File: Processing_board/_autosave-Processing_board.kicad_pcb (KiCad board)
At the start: 4 copper layers, 95.2 x 62 mm, 116 parts, among them J1 Conn_01x08_Pin, J10 Conn_01x03_Pin, J11 CONMHF1-SMD-G-T, J2 Conn_01x08_Pin, J3 Conn_01x06_Pin, J4 Conn_01x03_Pin, J5 Conn_01x03_Pin, J6 Conn_01x02_Pin, J7 Conn_01x02_Pin, J8 USB4215-03-A_REVA, J9 Conn_01x03_Pin, Q1 DMN66D0LT-7, Q2 DMN66D0LT-7, Q3 DMP3056LSS-13, SW1 TL3305BF100QG, SW2 TL3305BF100QG, U1 STM32WBA63CIU6, U2 MCP2200-I_SO, U3 LD1117S50TR_SOT223, U4 LD1117S33TR_SOT223, U5 LD1117DT18TR, U6 BGS13SN8E6327XTSA1, U7 OPA192IDR, U8 REF5025AQDRQ1, U9 ADS7953SBDBT

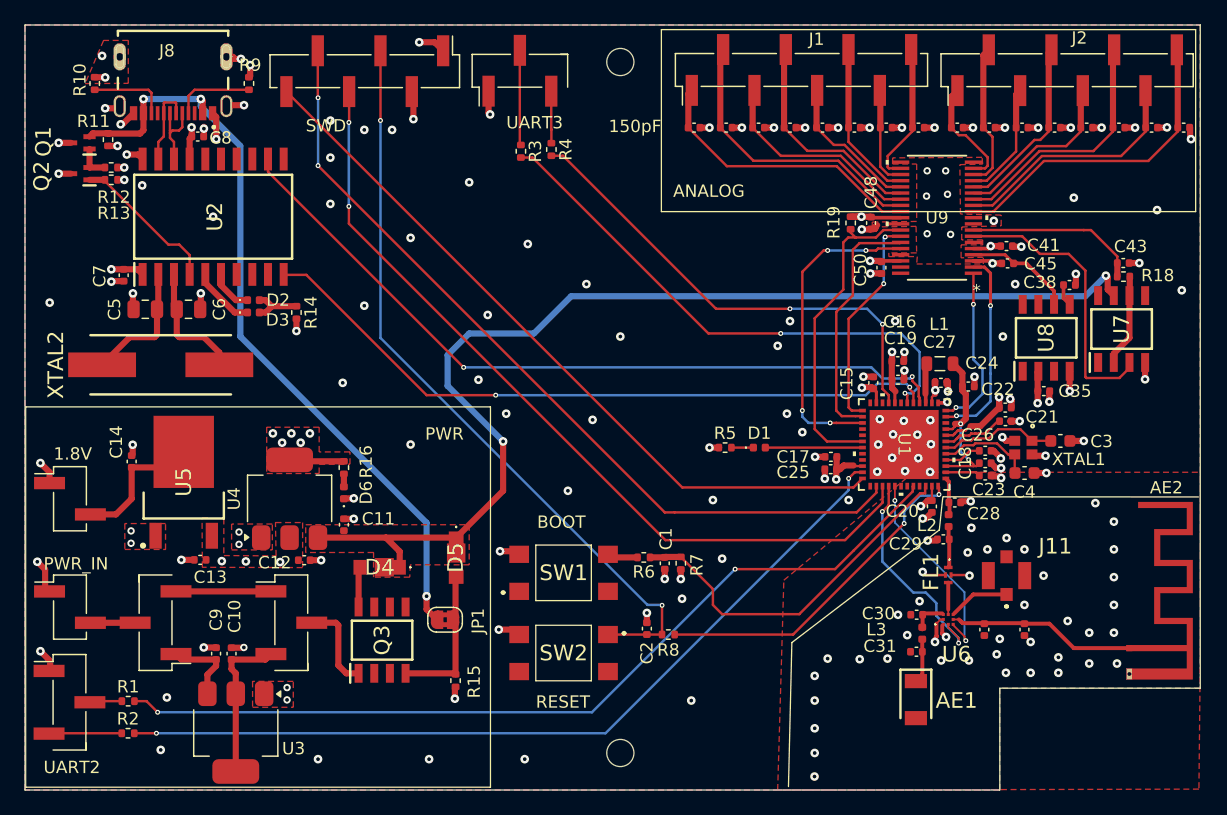
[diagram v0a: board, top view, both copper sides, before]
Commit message: minor changes to correct DRC warnings
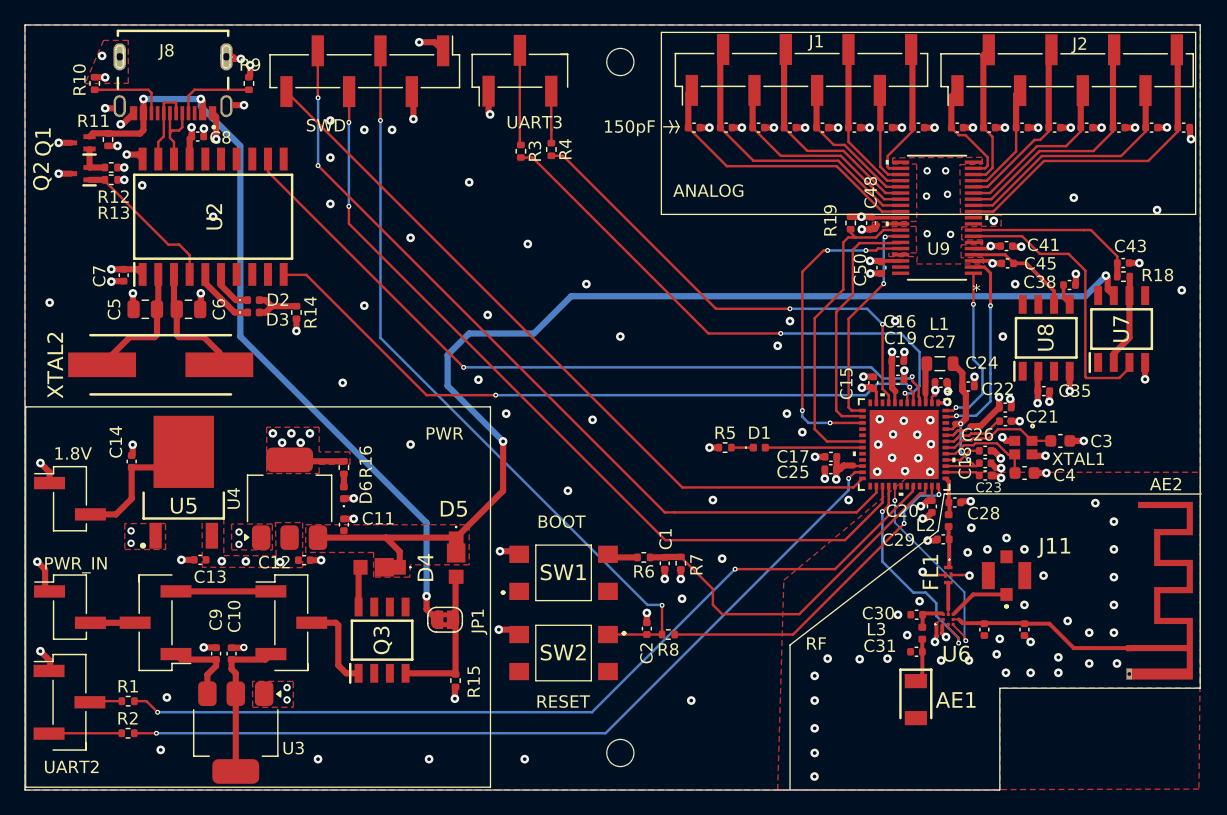
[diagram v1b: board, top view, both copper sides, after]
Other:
- board text added: "RF"
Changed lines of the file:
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@@
 		(tags "PCB antenna")
 		(property "Reference" "AE2"
-			(at -13 -3 180)
+			(at -13.25 -3 180)
 			(layer "F.SilkS")
 			(effects
@@
 		(tags "capacitor")
 		(property "Reference" "C29"
-			(at 3.074651 -0.367158 180)
+			(at 3.624651 -0.067158 180)
 			(layer "F.SilkS")
 			(effects
@@
 		(tags "capacitor")
 		(property "Reference" "C4"
-			(at 0.01 -1.54 0)
+			(at -3.24 -0.19 0)
 			(layer "F.SilkS")
 			(effects
@@
 		(tags "ADS7953SBDBT ")
 		(property "Reference" "U9"
-			(at 0 0 0)
+			(at -0.134931 -2.530498 0)
 			(unlocked yes)
 			(layer "F.SilkS")
@@
 		(tags "Integrated Circuit")
 		(property "Reference" "U5"
-			(at 0 0 90)
+			(at -1.955 0 180)
 			(layer "F.SilkS")
 			(effects
@@
 			(pinfunction "GND_A")
 			(pintype "power_in")
-			(solder_mask_margin 0.102)
+			(solder_mask_margin 0.09)
 		)
 		(pad "A4_B9" smd rect
@@
 			(pinfunction "VBUS_A")
 			(pintype "power_in")
-			(solder_mask_margin 0.102)
+			(solder_mask_margin 0.09)
 		)
 		(pad "A5" smd rect
@@
 			(pinfunction "CC1")
 			(pintype "bidirectional")
-			(solder_mask_margin 0.102)
+			(solder_mask_margin 0.09)
 		)
 		(pad "A6" smd rect
@@
 			(pinfunction "D+")
 			(pintype "bidirectional")
-			(solder_mask_margin 0.102)
+			(solder_mask_margin 0.09)
 		)
 		(pad "A7" smd rect
@@
 			(pinfunction "D-")
 			(pintype "bidirectional")
-			(solder_mask_margin 0.102)
+			(solder_mask_margin 0.09)
 		)
 		(pad "A8" smd rect
@@
 			(pinfunction "SBU1")
 			(pintype "bidirectional+no_connect")
-			(solder_mask_margin 0.102)
+			(solder_mask_margin 0.09)
 		)
 		(pad "B1_A12" smd rect
@@
 			(pinfunction "GND_B")
 			(pintype "power_in")
-			(solder_mask_margin 0.102)
+			(solder_mask_margin 0.09)
 		)
 		(pad "B4_A9" smd rect
@@
 			(pinfunction "VBUS_B")
 			(pintype "power_in")
-			(solder_mask_margin 0.102)
+			(solder_mask_margin 0.09)
 		)
 		(pad "B5" smd rect
@@
 			(pinfunction "CC2")
 			(pintype "bidirectional")
-			(solder_mask_margin 0.102)
+			(solder_mask_margin 0.09)
 		)
 		(pad "B6" smd rect
@@
 			(pinfunction "D+")
 			(pintype "bidirectional")
-			(solder_mask_margin 0.102)
+			(solder_mask_margin 0.09)
 		)
 		(pad "B7" smd rect
@@
 			(pinfunction "D-")
 			(pintype "bidirectional")
-			(solder_mask_margin 0.102)
+			(solder_mask_margin 0.09)
 		)
 		(pad "B8" smd rect
@@
 			(pinfunction "SBU2")
 			(pintype "bidirectional+no_connect")
-			(solder_mask_margin 0.102)
+			(solder_mask_margin 0.09)
 		)
 		(pad "SH1" thru_hole oval
@@
 		(tags "STM32WBA63CIU6 ")
 		(property "Reference" "U1"
-			(at 0 0 270)
+			(at 0.1 -0.1 0)
 			(unlocked yes)
 			(layer "F.SilkS")
+			(hide yes)
 			(effects
 				(font
@@
 		(tags "capacitor")
 		(property "Reference" "C23"
-			(at -0.28 -1.14 0)
+			(at -0.28 -0.99 0)
 			(layer "F.SilkS")
 			(effects
 				(font
-					(size 1 1)
+					(size 0.8 0.8)
 					(thickness 0.15)
 				)
@@
 		(tags "resistor")
 		(property "Reference" "R19"
-			(at -0.044503 1.365017 90)
+			(at -0.194503 1.615017 90)
 			(layer "F.SilkS")
 			(effects
@@
 		(tags "Schottky Diode")
 		(property "Reference" "D5"
-			(at 0.037 0.05 90)
+			(at -3.882 0.195 180)
 			(layer "F.SilkS")
 			(effects
@@
 		(tags "Surface mounted pin header SMD 1x08 2.54mm single row style1 pin1 left")
 		(property "Reference" "J2"
-			(at 2.614503 0.989983 0)
+			(at 2.114503 1.039983 0)
 			(layer "F.SilkS")
 			(effects
@@
 		(tags "inductor")
 		(property "Reference" "L2"
-			(at 0.382158 1.754651 180)
+			(at 0.382158 1.854651 180)
 			(layer "F.SilkS")
 			(effects
@@
 		(tags "Surface mounted pin header SMD 1x08 2.54mm single row style1 pin1 left")
 		(property "Reference" "J1"
-			(at 2.494503 1.219983 180)
+			(at 2.294503 1.219983 180)
 			(layer "F.SilkS")
 			(effects
@@
 		(tags "Schottky Diode")
 		(property "Reference" "D4"
-			(at 0.037 0 0)
+			(at -3.718 -0.049 270)
 			(layer "F.SilkS")
 			(effects
@@
 		)
 	)
+	(gr_line
+		(start 130.5 74.25)
+		(end 131.75 74.25)
+		(stroke
+			(width 0.1)
+			(type default)
+		)
+		(layer "F.SilkS")
+	)
 	(gr_rect
-		(start 130.325 66.375)
-		(end 173.625 81.125)
+		(start 130.325 66.6)
+		(end 173.625 81.35)
 		(stroke
 			(width 0.1)
@@
 	)
 	(gr_line
-		(start 153.195 104.238)
-		(end 173.85 104.25)
+		(start 153.4225 104)
+		(end 174.0775 104.012)
 		(stroke
 			(width 0.1)
@@
 		(layer "F.SilkS")
 	)
-	(gr_rect
-		(start 78.804724 96.949622)
-		(end 116.475 127.775)
+	(gr_line
+		(start 131.75 74.25)
+		(end 131.5 74.75)
 		(stroke
 			(width 0.1)
 			(type default)
 		)
-		(fill no)
 		(layer "F.SilkS")
 	)
 	(gr_line
-		(start 153.134651 104.238)
-		(end 152.85 106.925)
+		(start 153.5 104)
+		(end 153.25 104)
 		(stroke
 			(width 0.1)
@@
 		(layer "F.SilkS")
 	)
-	(gr_line
-		(start 152.85 106.925)
-		(end 140.9 116.05)
+	(gr_rect
+		(start 78.804724 96.949622)
+		(end 116.475 127.775)
 		(stroke
 			(width 0.1)
 			(type default)
 		)
+		(fill no)
 		(layer "F.SilkS")
 	)
 	(gr_line
-		(start 140.9 116.05)
-		(end 140.625 127.725)
+		(start 131.75 74.25)
+		(end 131.5 73.75)
 		(stroke
 			(width 0.1)
@@
 	)
 	(gr_line
-		(start 131.25 74.2)
-		(end 131.1 74.45)
+		(start 140.75 116.25)
+		(end 140.75 128)
 		(stroke
 			(width 0.1)
 			(type default)
 		)
-		(layer "F.Paste")
+		(layer "F.SilkS")
 	)
 	(gr_line
-		(start 131.75 74.2)
-		(end 131.5 73.9)
+		(start 131.25 74.25)
+		(end 131 74.75)
 		(stroke
 			(width 0.1)
 			(type default)
 		)
-		(layer "F.Paste")
+		(layer "F.SilkS")
 	)
 	(gr_line
-		(start 130.75 74.2)
-		(end 131.75 74.2)
+		(start 131.25 74.25)
+		(end 131 73.75)
 		(stroke
 			(width 0.1)
 			(type default)
 		)
-		(layer "F.Paste")
+		(layer "F.SilkS")
 	)
 	(gr_line
-		(start 131.75 74.2)
-		(end 131.5 74.5)
+		(start 152.75 107)
+		(end 140.75 116.25)
 		(stroke
 			(width 0.1)
 			(type default)
 		)
-		(layer "F.Paste")
+		(layer "F.SilkS")
 	)
 	(gr_line
-		(start 131.25 74.2)
-		(end 131.1 73.95)
+		(start 153.25 104)
+		(end 152.75 107)
 		(stroke
 			(width 0.1)
 			(type default)
 		)
-		(layer "F.Paste")
+		(layer "F.SilkS")
 	)
 	(gr_rect
@@
 		)
 	)
+	(gr_text "RF"
+		(at 142 116.75 0)
+		(layer "F.SilkS")
+		(effects
+			(font
+				(size 1 1)
+				(thickness 0.1)
+			)
+			(justify left bottom)
+		)
+	)
 	(gr_text "PWR_IN"
 		(at 80.25 110.25 0)
@@
 	)
 	(gr_text "150pF"
-		(at 126.05 74.8 0)
+		(at 125.6 74.85 0)
 		(layer "F.SilkS")
 		(effects
@@
 	)
 	(segment
-		(start 151.496003 114.945842)
-		(end 151.466003 114.975842)
-		(width 0.3208)
-		(layer "F.Cu")
-		(net 4)
-	)
-	(segment
 		(start 151.602403 113.689442)
 		(end 153.088251 113.689442)
@@
 	)
 	(segment
-		(start 151.441003 114.950842)
-		(end 151.466003 114.975842)
-		(width 0.3208)
-		(layer "F.Cu")
-		(net 4)
-	)
-	(segment
 		(start 151.496003 113.795842)
 		(end 151.496003 114.780842)
@@
 		(width 0.2)
 		(layer "F.Cu")
-		(net 13)
-	)
-	(segment
-		(start 154.513534 99.273001)
-		(end 154.513535 99.273001)
-		(width 0.2)
-		(layer "F.Cu")
